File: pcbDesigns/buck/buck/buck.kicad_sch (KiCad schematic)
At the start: 15 parts, among them J1 GND, J2 5V, J3 ESP_CONNECTOR, J4 RECTIFIER_IN, J5 PWM_OUT, J6 CURR_SENS, Q1 IXGH24N60C4D1, U1 TLP250

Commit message: designed pcb for the buck
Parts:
- C1: footprint (none) -> Capacitor_THT:CP_Radial_D35.0mm_P10.00mm_SnapIn
- C2: footprint (none) -> Capacitor_THT:C_Disc_D5.1mm_W3.2mm_P5.00mm
- D1: footprint (none) -> Package_TO_SOT_THT:TO-247-2_Vertical
- F1: footprint (none) -> Fuse:Fuseholder_Cylinder-5x20mm_Schurter_0031_8201_Horizontal_Open
- J1, J2: footprint (none) -> Connector_PinHeader_2.54mm:PinHeader_1x06_P2.54mm_Vertical
- J3: footprint (none) -> Connector_PinHeader_2.54mm:PinHeader_1x02_P2.54mm_Vertical
- J4, J5, J6: footprint (none) -> TerminalBlock_MetzConnect:TerminalBlock_MetzConnect_Type175_RT02702HBLC_1x02_P7.50mm_Horizontal
- PS1: footprint CONV_ROE-0512S -> Module:roe0512
- R1, R2: footprint (none) -> Resistor_THT:R_Axial_DIN0204_L3.6mm_D1.6mm_P7.62mm_Horizontal
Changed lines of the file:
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@@
       (effects (font (size 1.27 1.27)) (justify left))
     )
-    (property "Footprint" "" (id 2) (at 247.65 68.58 0)
+    (property "Footprint" "TerminalBlock_MetzConnect:TerminalBlock_MetzConnect_Type175_RT02702HBLC_1x02_P7.50mm_Horizontal" (id 2) (at 247.65 68.58 0)
       (effects (font (size 1.27 1.27)) hide)
     )
@@
     (property "Reference" "J4" (id 0) (at 109.22 45.72 0))
     (property "Value" "RECTIFIER_IN" (id 1) (at 109.22 48.26 0))
-    (property "Footprint" "" (id 2) (at 109.22 52.07 0)
+    (property "Footprint" "TerminalBlock_MetzConnect:TerminalBlock_MetzConnect_Type175_RT02702HBLC_1x02_P7.50mm_Horizontal" (id 2) (at 109.22 52.07 0)
       (effects (font (size 1.27 1.27)) hide)
     )
@@
     (property "Reference" "PS1" (id 0) (at 128.27 96.52 0))
     (property "Value" "ROE-0512S" (id 1) (at 128.27 99.06 0))
-    (property "Footprint" "CONV_ROE-0512S" (id 2) (at 128.27 109.22 0)
+    (property "Footprint" "Module:roe0512" (id 2) (at 128.27 109.22 0)
       (effects (font (size 1.27 1.27)) (justify bottom) hide)
     )
@@
       (effects (font (size 1.27 1.27)) (justify left))
     )
-    (property "Footprint" "" (id 2) (at 136.8552 57.15 0)
+    (property "Footprint" "Capacitor_THT:C_Disc_D5.1mm_W3.2mm_P5.00mm" (id 2) (at 136.8552 57.15 0)
       (effects (font (size 1.27 1.27)) hide)
     )
@@
     (property "Reference" "J1" (id 0) (at 74.295 100.33 0))
     (property "Value" "GND" (id 1) (at 74.295 102.87 0))
-    (property "Footprint" "" (id 2) (at 73.66 110.49 0)
+    (property "Footprint" "Connector_PinHeader_2.54mm:PinHeader_1x06_P2.54mm_Vertical" (id 2) (at 73.66 110.49 0)
       (effects (font (size 1.27 1.27)) hide)
     )
@@
     (property "Reference" "J2" (id 0) (at 75.565 38.1 0))
     (property "Value" "5V" (id 1) (at 75.565 40.64 0))
-    (property "Footprint" "" (id 2) (at 74.93 48.26 0)
+    (property "Footprint" "Connector_PinHeader_2.54mm:PinHeader_1x06_P2.54mm_Vertical" (id 2) (at 74.93 48.26 0)
       (effects (font (size 1.27 1.27)) hide)
     )
@@
     (property "Reference" "F1" (id 0) (at 146.05 35.56 90))
     (property "Value" "Fuse" (id 1) (at 146.05 38.1 90))
-    (property "Footprint" "" (id 2) (at 146.05 43.688 90)
+    (property "Footprint" "Fuse:Fuseholder_Cylinder-5x20mm_Schurter_0031_8201_Horizontal_Open" (id 2) (at 146.05 43.688 90)
       (effects (font (size 1.27 1.27)) hide)
     )
@@
     (property "Reference" "J3" (id 0) (at 75.565 71.12 0))
     (property "Value" "ESP_CONNECTOR" (id 1) (at 75.565 73.66 0))
-    (property "Footprint" "" (id 2) (at 74.93 76.2 0)
+    (property "Footprint" "Connector_PinHeader_2.54mm:PinHeader_1x02_P2.54mm_Vertical" (id 2) (at 74.93 76.2 0)
       (effects (font (size 1.27 1.27)) hide)
     )
@@
       (effects (font (size 1.27 1.27)) (justify right))
     )
-    (property "Footprint" "" (id 2) (at 226.06 55.88 0)
+    (property "Footprint" "Package_TO_SOT_THT:TO-247-2_Vertical" (id 2) (at 226.06 55.88 0)
       (effects (font (size 1.27 1.27)) hide)
     )
@@
       (effects (font (size 1.27 1.27)) (justify left))
     )
-    (property "Footprint" "" (id 2) (at 247.65 59.69 0)
+    (property "Footprint" "TerminalBlock_MetzConnect:TerminalBlock_MetzConnect_Type175_RT02702HBLC_1x02_P7.50mm_Horizontal" (id 2) (at 247.65 59.69 0)
       (effects (font (size 1.27 1.27)) hide)
     )
@@
       (effects (font (size 1.27 1.27)) (justify left))
     )
-    (property "Footprint" "" (id 2) (at 124.46 53.34 0)
+    (property "Footprint" "Capacitor_THT:CP_Radial_D35.0mm_P10.00mm_SnapIn" (id 2) (at 124.46 53.34 0)
       (effects (font (size 1.27 1.27)) hide)
     )
@@
     (property "Reference" "R2" (id 0) (at 222.25 76.2 90))
     (property "Value" "R_GATE" (id 1) (at 222.25 78.74 90))
-    (property "Footprint" "" (id 2) (at 222.504 81.534 90)
+    (property "Footprint" "Resistor_THT:R_Axial_DIN0204_L3.6mm_D1.6mm_P7.62mm_Horizontal" (id 2) (at 222.504 81.534 90)
       (effects (font (size 1.27 1.27)) hide)
     )
@@
     (property "Reference" "R1" (id 0) (at 179.07 68.58 90))
     (property "Value" "R_OPTO" (id 1) (at 179.07 71.12 90))
-    (property "Footprint" "" (id 2) (at 179.324 73.914 90)
+    (property "Footprint" "Resistor_THT:R_Axial_DIN0204_L3.6mm_D1.6mm_P7.62mm_Horizontal" (id 2) (at 179.324 73.914 90)
       (effects (font (size 1.27 1.27)) hide)
     )
@@
     )
     (path "/bbdc68c7-50a5-452a-887e-b80055ad1157"
-      (reference "C1") (unit 1) (value "680u") (footprint "")
+      (reference "C1") (unit 1) (value "680u") (footprint "Capacitor_THT:CP_Radial_D35.0mm_P10.00mm_SnapIn")
     )
     (path "/1f5a3425-ef2b-4762-b46e-625afed4b01f"
-      (reference "C2") (unit 1) (value "10n") (footprint "")
+      (reference "C2") (unit 1) (value "10n") (footprint "Capacitor_THT:C_Disc_D5.1mm_W3.2mm_P5.00mm")
     )
     (path "/ac0283f4-001b-44ee-8f26-69af52043178"
-      (reference "D1") (unit 1) (value "DSEI30-06A") (footprint "")
+      (reference "D1") (unit 1) (value "DSEI30-06A") (footprint "Package_TO_SOT_THT:TO-247-2_Vertical")
     )
     (path "/8207a9e9-644b-46e5-9b27-6e3e59e9bb7d"
-      (reference "F1") (unit 1) (value "Fuse") (footprint "")
+      (reference "F1") (unit 1) (value "Fuse") (footprint "Fuse:Fuseholder_Cylinder-5x20mm_Schurter_0031_8201_Horizontal_Open")
     )
     (path "/3e334304-64cf-451c-9c42-7b69e30eff7c"
-      (reference "J1") (unit 1) (value "GND") (footprint "")
+      (reference "J1") (unit 1) (value "GND") (footprint "Connector_PinHeader_2.54mm:PinHeader_1x06_P2.54mm_Vertical")
     )
     (path "/52a9df48-000d-4f4c-ba68-05405d5989c2"
-      (reference "J2") (unit 1) (value "5V") (footprint "")
+      (reference "J2") (unit 1) (value "5V") (footprint "Connector_PinHeader_2.54mm:PinHeader_1x06_P2.54mm_Vertical")
     )
     (path "/9b0c9466-402b-4227-a5e8-3fe3f042c1db"
-      (reference "J3") (unit 1) (value "ESP_CONNECTOR") (footprint "")
+      (reference "J3") (unit 1) (value "ESP_CONNECTOR") (footprint "Connector_PinHeader_2.54mm:PinHeader_1x02_P2.54mm_Vertical")
     )
     (path "/1a907062-f9a9-45b4-b3a9-85b763e3ec8b"
-      (reference "J4") (unit 1) (value "RECTIFIER_IN") (footprint "")
+      (reference "J4") (unit 1) (value "RECTIFIER_IN") (footprint "TerminalBlock_MetzConnect:TerminalBlock_MetzConnect_Type175_RT02702HBLC_1x02_P7.50mm_Horizontal")
     )
     (path "/b9ccdaf3-44a4-4cc5-b805-59b049cb7354"
-      (reference "J5") (unit 1) (value "PWM_OUT") (footprint "")
+      (reference "J5") (unit 1) (value "PWM_OUT") (footprint "TerminalBlock_MetzConnect:TerminalBlock_MetzConnect_Type175_RT02702HBLC_1x02_P7.50mm_Horizontal")
     )
     (path "/0169e3be-ab0c-49d2-b9ed-109a4a14c7af"
-      (reference "J6") (unit 1) (value "CURR_SENS") (footprint "")
+      (reference "J6") (unit 1) (value "CURR_SENS") (footprint "TerminalBlock_MetzConnect:TerminalBlock_MetzConnect_Type175_RT02702HBLC_1x02_P7.50mm_Horizontal")
     )
     (path "/1f49196a-7b05-41a0-b299-51f9e6c45aec"
-      (reference "PS1") (unit 1) (value "ROE-0512S") (footprint "CONV_ROE-0512S")
+      (reference "PS1") (unit 1) (value "ROE-0512S") (footprint "Module:roe0512")
     )
     (path "/4b91a28b-e778-4691-8d2b-bb09bc10e8e8"
@@
     )
     (path "/ebf90cdd-4571-49f6-a001-244714ee23b7"
-      (reference "R1") (unit 1) (value "R_OPTO") (footprint "")
+      (reference "R1") (unit 1) (value "R_OPTO") (footprint "Resistor_THT:R_Axial_DIN0204_L3.6mm_D1.6mm_P7.62mm_Horizontal")
     )
     (path "/c22652a6-5a32-4599-a80e-89273289b919"
-      (reference "R2") (unit 1) (value "R_GATE") (footprint "")
+      (reference "R2") (unit 1) (value "R_GATE") (footprint "Resistor_THT:R_Axial_DIN0204_L3.6mm_D1.6mm_P7.62mm_Horizontal")
     )
     (path "/9d89eb5e-6285-4416-b4d6-f808b388a814"

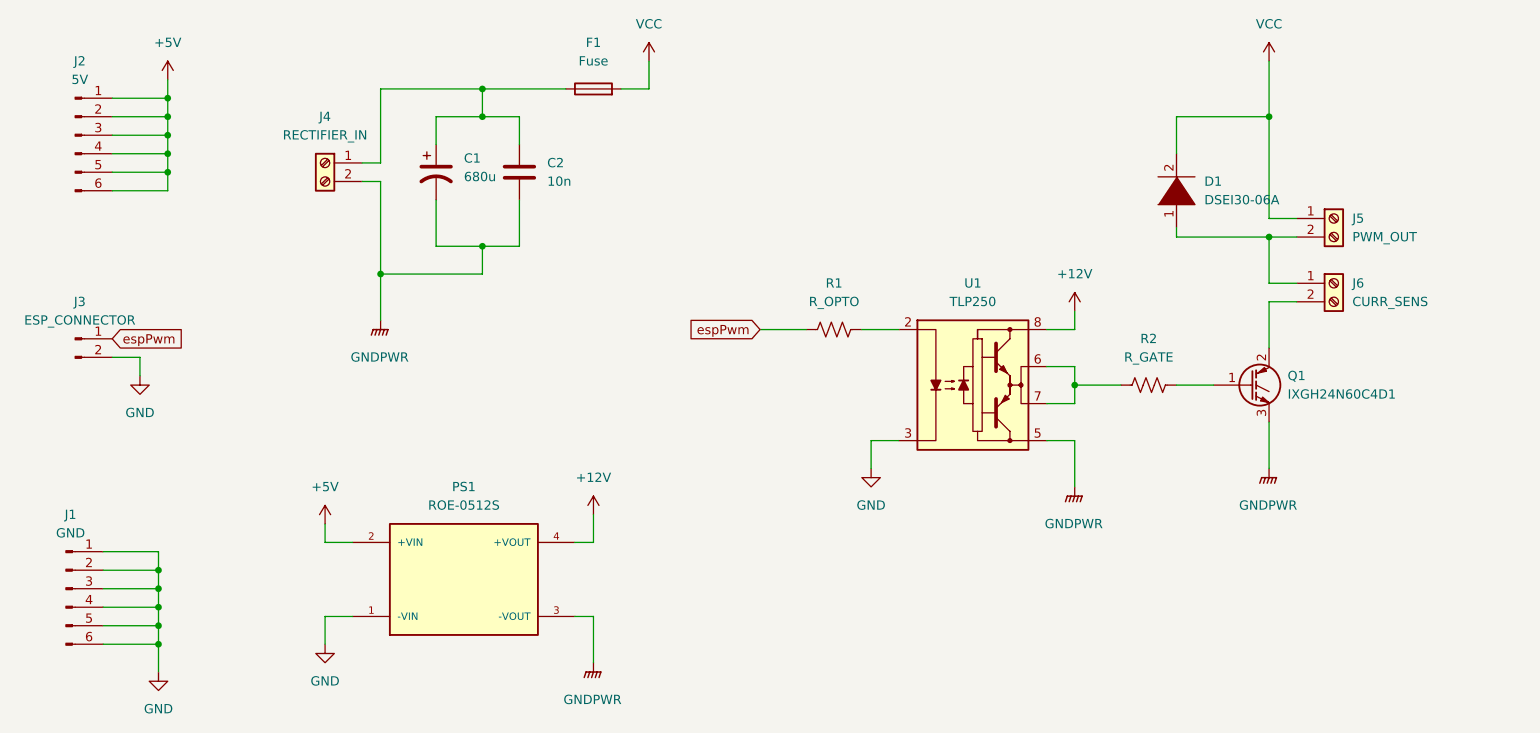
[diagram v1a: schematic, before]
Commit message: add resistor and correct capacitor values
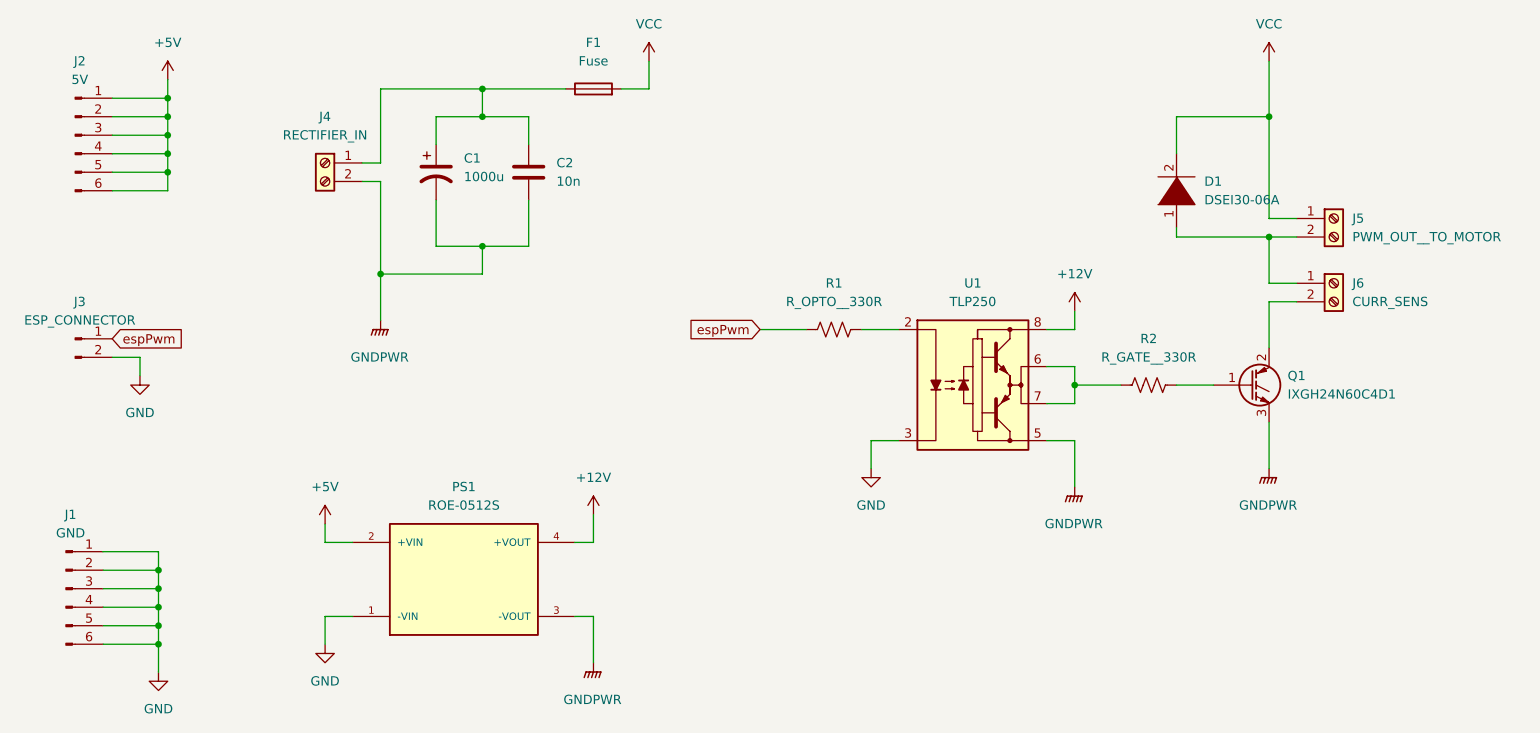
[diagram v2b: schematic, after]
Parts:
- C1: value 680u -> 1000u
- J5: value PWM_OUT -> PWM_OUT__TO_MOTOR
- R1: value R_OPTO -> R_OPTO__330R
- R2: value R_GATE -> R_GATE__330R
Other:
- moved on the sheet: C2
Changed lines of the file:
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@@
     (stroke (width 0) (type default) (color 0 0 0 0))
   )
-  (wire (pts (xy 130.81 45.72) (xy 135.89 45.72))
+  (wire (pts (xy 130.81 45.72) (xy 137.16 45.72))
     (stroke (width 0) (type default) (color 0 0 0 0))
   )
@@
     (stroke (width 0) (type default) (color 0 0 0 0))
   )
-  (wire (pts (xy 135.89 57.15) (xy 135.89 63.5))
-    (stroke (width 0) (type default) (color 0 0 0 0))
-  )
-  (wire (pts (xy 135.89 45.72) (xy 135.89 49.53))
+  (wire (pts (xy 137.16 57.15) (xy 137.16 63.5))
+    (stroke (width 0) (type default) (color 0 0 0 0))
+  )
+  (wire (pts (xy 137.16 45.72) (xy 137.16 49.53))
     (stroke (width 0) (type default) (color 0 0 0 0))
   )
@@
     (stroke (width 0) (type default) (color 0 0 0 0))
   )
-  (wire (pts (xy 130.81 63.5) (xy 135.89 63.5))
+  (wire (pts (xy 130.81 63.5) (xy 137.16 63.5))
     (stroke (width 0) (type default) (color 0 0 0 0))
   )
@@
     (pin "4")
   )
-  (symbol (lib_id "Device:C") (at 135.89 53.34 0) (unit 1)
-    (in_bom yes) (on_board yes) (fields_autoplaced)
-    (property "Reference" "C2" (id 0) (at 139.7 52.0699 0)
-      (effects (font (size 1.27 1.27)) (justify left))
-    )
-    (property "Value" "10n" (id 1) (at 139.7 54.6099 0)
-      (effects (font (size 1.27 1.27)) (justify left))
-    )
-    (property "Footprint" "Capacitor_THT:C_Disc_D5.1mm_W3.2mm_P5.00mm" (id 2) (at 136.8552 57.15 0)
-      (effects (font (size 1.27 1.27)) hide)
-    )
-    (property "Datasheet" "~" (id 3) (at 135.89 53.34 0)
+  (symbol (lib_id "Device:C") (at 137.16 53.34 0) (unit 1)
+    (in_bom yes) (on_board yes) (fields_autoplaced)
+    (property "Reference" "C2" (id 0) (at 140.97 52.0699 0)
+      (effects (font (size 1.27 1.27)) (justify left))
+    )
+    (property "Value" "10n" (id 1) (at 140.97 54.6099 0)
+      (effects (font (size 1.27 1.27)) (justify left))
+    )
+    (property "Footprint" "Capacitor_THT:C_Disc_D5.1mm_W3.2mm_P5.00mm" (id 2) (at 138.1252 57.15 0)
+      (effects (font (size 1.27 1.27)) hide)
+    )
+    (property "Datasheet" "~" (id 3) (at 137.16 53.34 0)
       (effects (font (size 1.27 1.27)) hide)
     )
@@
       (effects (font (size 1.27 1.27)) (justify left))
     )
-    (property "Value" "PWM_OUT" (id 1) (at 250.19 62.2299 0)
+    (property "Value" "PWM_OUT__TO_MOTOR" (id 1) (at 250.19 62.2299 0)
       (effects (font (size 1.27 1.27)) (justify left))
     )
@@
       (effects (font (size 1.27 1.27)) (justify left))
     )
-    (property "Value" "680u" (id 1) (at 128.27 53.9749 0)
+    (property "Value" "1000u" (id 1) (at 128.27 53.9749 0)
       (effects (font (size 1.27 1.27)) (justify left))
     )
@@
     (in_bom yes) (on_board yes) (fields_autoplaced)
     (property "Reference" "R2" (id 0) (at 222.25 76.2 90))
-    (property "Value" "R_GATE" (id 1) (at 222.25 78.74 90))
+    (property "Value" "R_GATE__330R" (id 1) (at 222.25 78.74 90))
     (property "Footprint" "Resistor_THT:R_Axial_DIN0204_L3.6mm_D1.6mm_P7.62mm_Horizontal" (id 2) (at 222.504 81.534 90)
       (effects (font (size 1.27 1.27)) hide)
@@
     (in_bom yes) (on_board yes) (fields_autoplaced)
     (property "Reference" "R1" (id 0) (at 179.07 68.58 90))
-    (property "Value" "R_OPTO" (id 1) (at 179.07 71.12 90))
+    (property "Value" "R_OPTO__330R" (id 1) (at 179.07 71.12 90))
     (property "Footprint" "Resistor_THT:R_Axial_DIN0204_L3.6mm_D1.6mm_P7.62mm_Horizontal" (id 2) (at 179.324 73.914 90)
       (effects (font (size 1.27 1.27)) hide)
@@
     )
     (path "/bbdc68c7-50a5-452a-887e-b80055ad1157"
-      (reference "C1") (unit 1) (value "680u") (footprint "Capacitor_THT:CP_Radial_D35.0mm_P10.00mm_SnapIn")
+      (reference "C1") (unit 1) (value "1000u") (footprint "Capacitor_THT:CP_Radial_D35.0mm_P10.00mm_SnapIn")
     )
     (path "/1f5a3425-ef2b-4762-b46e-625afed4b01f"
@@
     )
     (path "/b9ccdaf3-44a4-4cc5-b805-59b049cb7354"
-      (reference "J5") (unit 1) (value "PWM_OUT") (footprint "TerminalBlock_MetzConnect:TerminalBlock_MetzConnect_Type175_RT02702HBLC_1x02_P7.50mm_Horizontal")
+      (reference "J5") (unit 1) (value "PWM_OUT__TO_MOTOR") (footprint "TerminalBlock_MetzConnect:TerminalBlock_MetzConnect_Type175_RT02702HBLC_1x02_P7.50mm_Horizontal")
     )
     (path "/0169e3be-ab0c-49d2-b9ed-109a4a14c7af"
@@
     )
     (path "/ebf90cdd-4571-49f6-a001-244714ee23b7"
-      (reference "R1") (unit 1) (value "R_OPTO") (footprint "Resistor_THT:R_Axial_DIN0204_L3.6mm_D1.6mm_P7.62mm_Horizontal")
+      (reference "R1") (unit 1) (value "R_OPTO__330R") (footprint "Resistor_THT:R_Axial_DIN0204_L3.6mm_D1.6mm_P7.62mm_Horizontal")
     )
     (path "/c22652a6-5a32-4599-a80e-89273289b919"
-      (reference "R2") (unit 1) (value "R_GATE") (footprint "Resistor_THT:R_Axial_DIN0204_L3.6mm_D1.6mm_P7.62mm_Horizontal")
+      (reference "R2") (unit 1) (value "R_GATE__330R") (footprint "Resistor_THT:R_Axial_DIN0204_L3.6mm_D1.6mm_P7.62mm_Horizontal")
     )
     (path "/9d89eb5e-6285-4416-b4d6-f808b388a814"
